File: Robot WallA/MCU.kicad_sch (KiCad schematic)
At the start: 0 parts

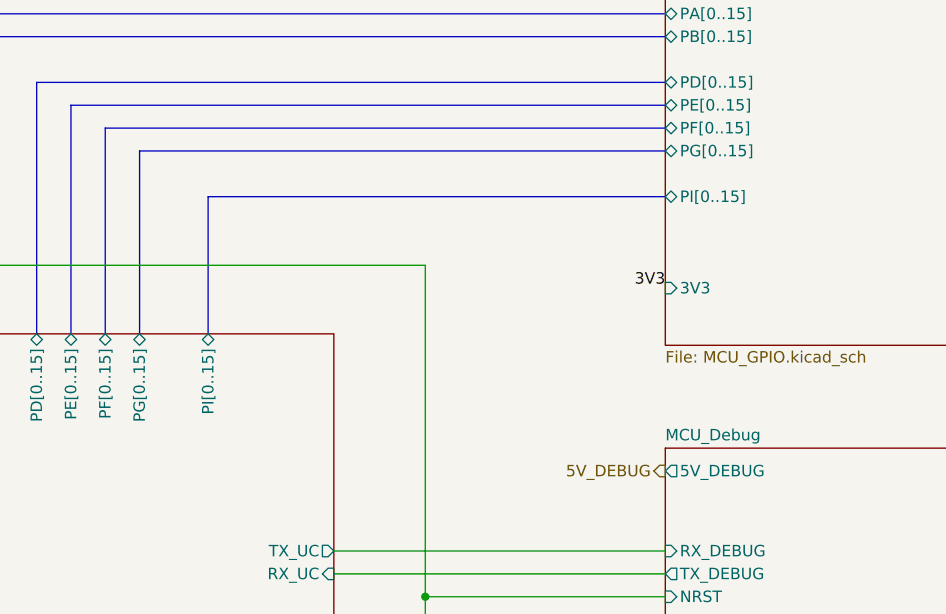
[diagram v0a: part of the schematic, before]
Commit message: Modified a bit pin header pins to allow I2C,SPI and CAN
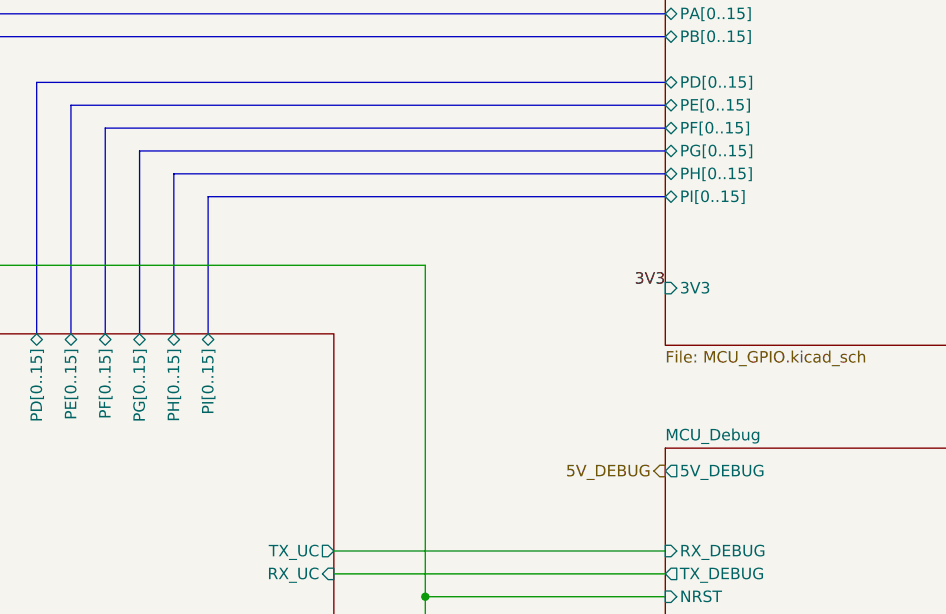
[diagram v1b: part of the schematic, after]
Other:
- sheet MCU_Core ports: added PH[0..15]; removed none
- sheet MCU_GPIO ports: added PH[0..15]; removed none
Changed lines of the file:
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@@
+		)
+	)
+	(bus
+		(pts
+			(xy 139.7 64.77) (xy 139.7 46.99)
+		)
+		(stroke
+			(width 0)
+			(type default)
 		)
 	)
@@
 		(pts
 			(xy 82.55 53.34) (xy 82.55 64.77)
+		)
+		(stroke
+			(width 0)
+			(type default)
+		)
+	)
+	(bus
+		(pts
+			(xy 139.7 46.99) (xy 194.31 46.99)
 		)
 		(stroke
@@
 			)
 		)
+		(pin "PH[0..15]" bidirectional
+			(at 139.7 64.77 90)
+			(effects
+				(font
+					(size 1.27 1.27)
+				)
+				(justify right)
+			)
+		)
 		(instances
 			(project "Robot WallA"
@@
 			(effects
 				(font
+					(size 1.27 1.27)
+				)
+				(justify left)
+			)
+		)
+		(pin "PH[0..15]" bidirectional
+			(at 194.31 46.99 180)
+			(effects
+				(font

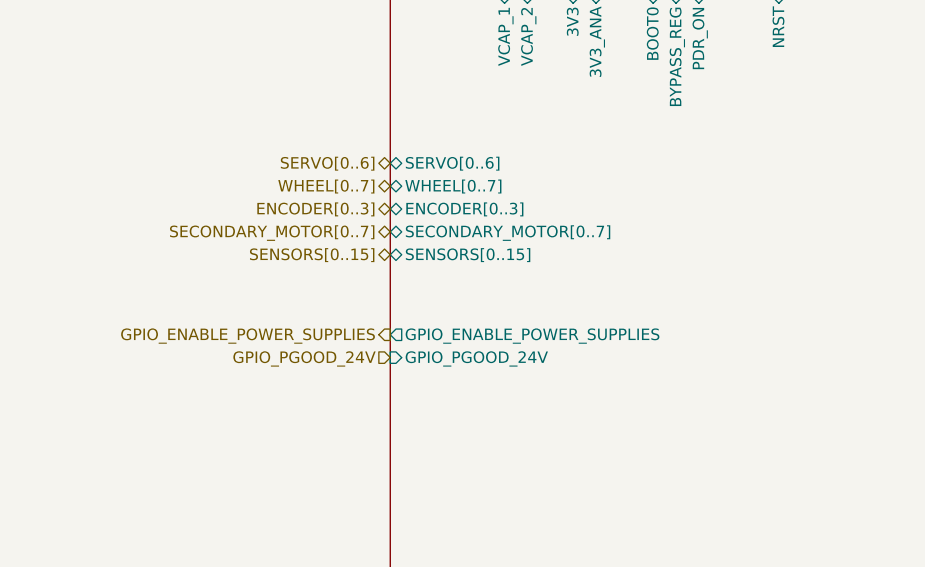
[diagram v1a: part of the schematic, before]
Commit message: Added 3 thermistor to measure temperature near 12V and 24V power supplies and near motor drivers
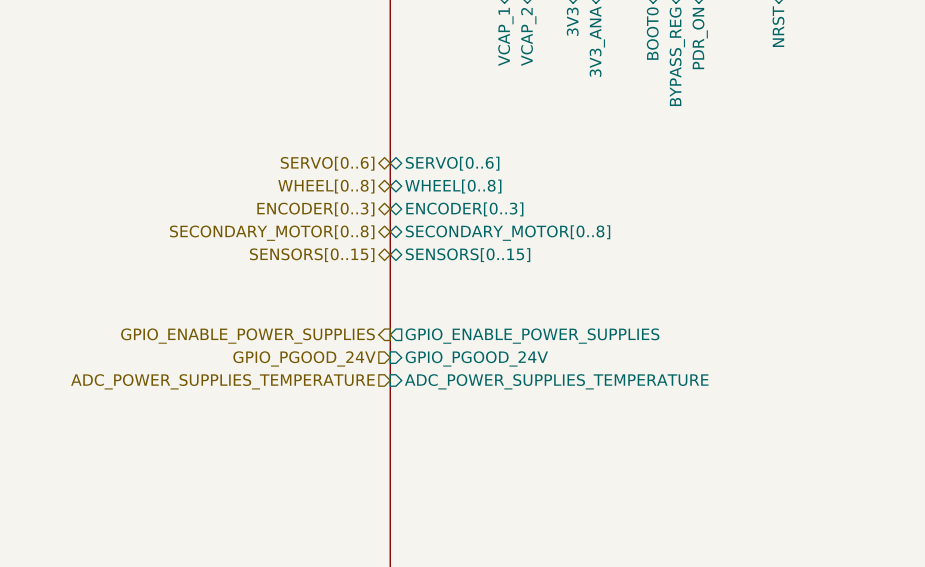
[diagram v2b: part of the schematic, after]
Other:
- sheet MCU_Core ports: added ADC_POWER_SUPPLIES_TEMPERATURE, SECONDARY_MOTOR[0..8], WHEEL[0..8]; removed SECONDARY_MOTOR[0..7], WHEEL[0..7]
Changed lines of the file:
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@@
 		)
 	)
-	(hierarchical_label "SECONDARY_MOTOR[0..7]"
+	(hierarchical_label "ADC_POWER_SUPPLIES_TEMPERATURE"
+		(shape input)
+		(at 48.26 107.95 180)
+		(effects
+			(font
+				(size 1.27 1.27)
+			)
+			(justify right)
+		)
+	)
+	(hierarchical_label "SECONDARY_MOTOR[0..8]"
 		(shape bidirectional)
 		(at 48.26 91.44 180)
@@
 		)
 	)
-	(hierarchical_label "WHEEL[0..7]"
+	(hierarchical_label "WHEEL[0..8]"
 		(shape bidirectional)
 		(at 48.26 86.36 180)
@@
 			)
 		)
-		(pin "WHEEL[0..7]" bidirectional
+		(pin "WHEEL[0..8]" bidirectional
 			(at 48.26 86.36 180)
 			(effects
@@
 			)
 		)
-		(pin "SECONDARY_MOTOR[0..7]" bidirectional
+		(pin "SECONDARY_MOTOR[0..8]" bidirectional
 			(at 48.26 91.44 180)
 			(effects
@@
 			)
 		)
+		(pin "ADC_POWER_SUPPLIES_TEMPERATURE" input
+			(at 48.26 107.95 180)
+			(effects
+				(font
+					(size 1.27 1.27)
+				)
+				(justify left)
+			)
+		)
